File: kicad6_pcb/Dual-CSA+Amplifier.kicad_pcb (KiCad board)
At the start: 2 copper layers, 101 x 69.2 mm, 87 parts, among them J101 Direct2 In, J102 CSA2 In, J103 CSA1 In, J104 Direct1 In, J105 Bias In, J106 Direct in, J107 Direct in, J108 Output, J109 Output, J201 Barrel_Jack, J202 GND, J203 DC Power, J204 -8V, J205 +8V, J301 CA probe, J302 RV Prob, J401 CA probe, J402 RV Prob, U201 LM317L, U202 UA78M08, U203 UA79M08, U204 TLE2426xP, U301 CR110, U302 TL071, U401 CR110, U402 TL071

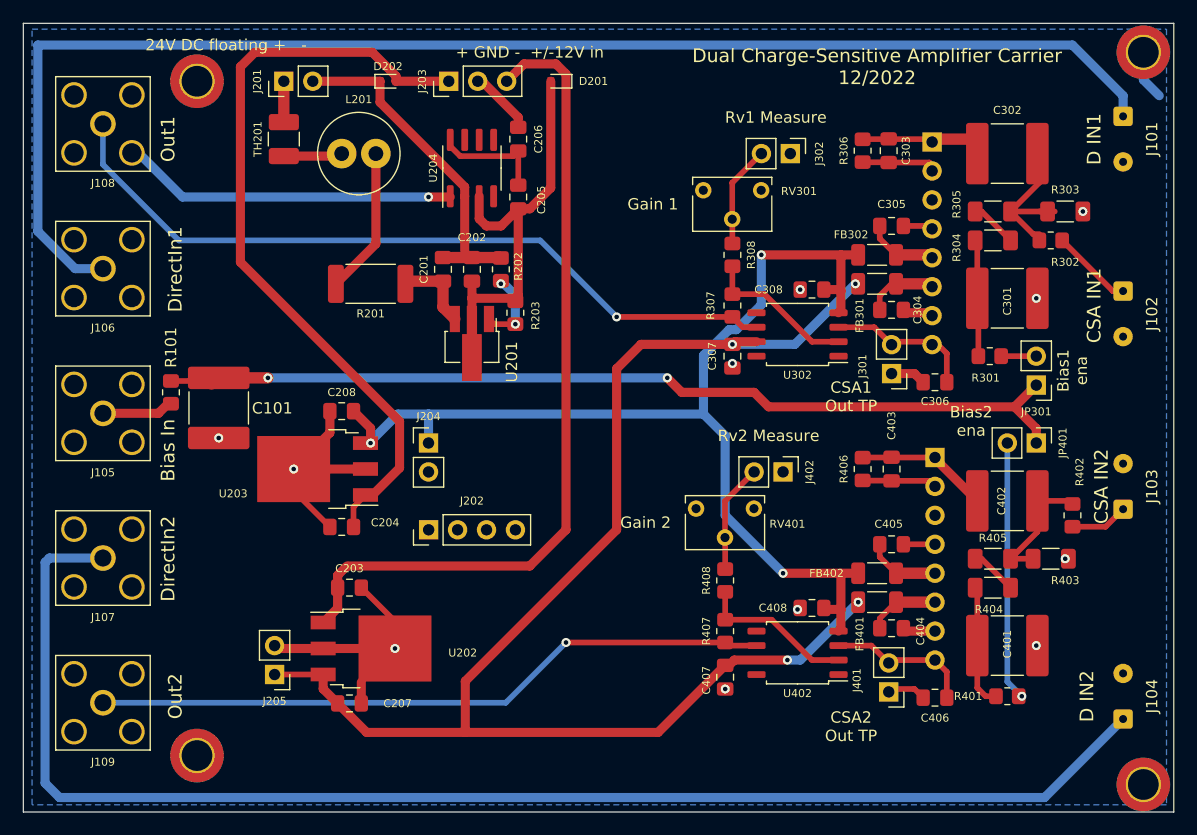
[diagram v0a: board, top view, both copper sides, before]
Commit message: CSA carrier v2. Multiple fixes and improvements.
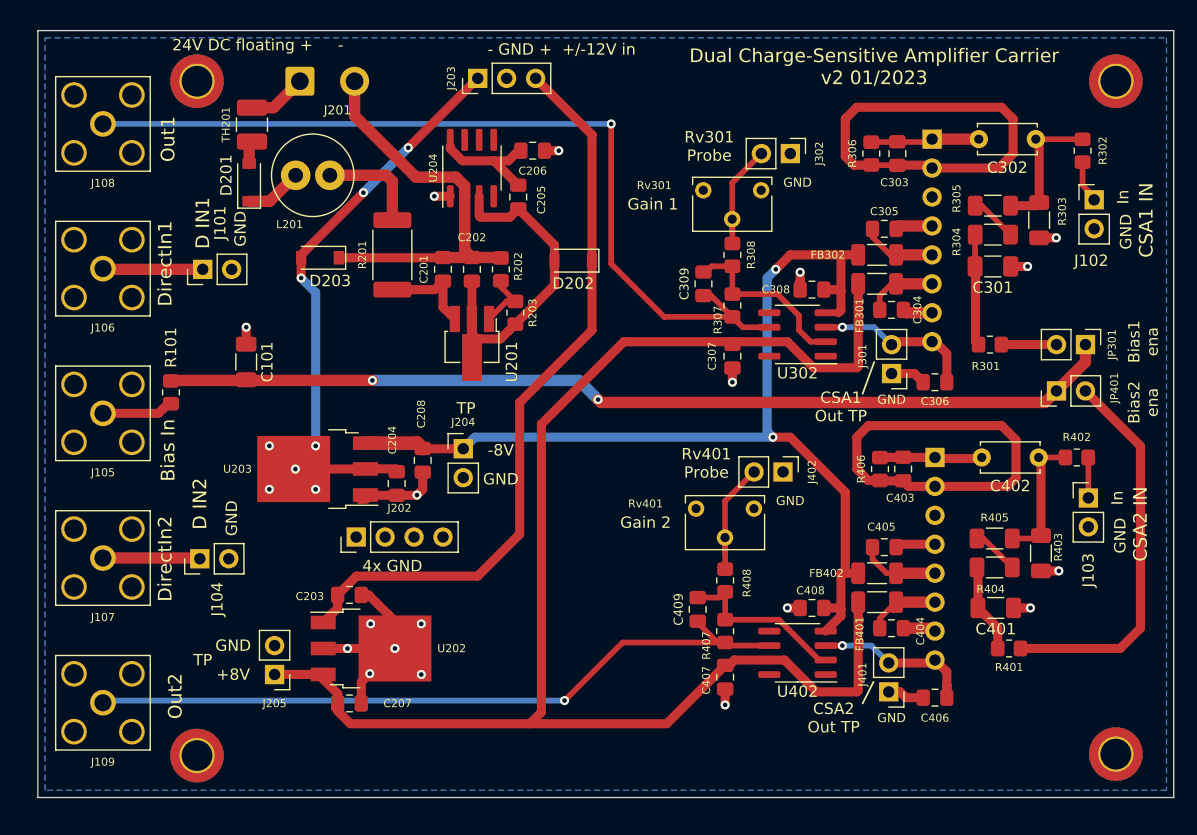
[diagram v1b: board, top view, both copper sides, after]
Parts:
- added C309: Open, Capacitor_SMD:C_0805_2012Metric_Pad1.18x1.45mm_HandSolder, F.Cu at (175.3, 114.3)
- added C409: Open, Capacitor_SMD:C_0805_2012Metric_Pad1.18x1.45mm_HandSolder, F.Cu at (174.8, 142.9)
- added D203: D, Diode_SMD:D_SOD-123, F.Cu at (141.6, 112.0)
- C101, C301, C401: footprint Capacitor_SMD:C_2220_5650Metric_Pad1.97x5.40mm_HandSolder -> Capacitor_SMD:C_1206_3216Metric_Pad1.33x1.80mm_HandSolder
- C302, C402: footprint Capacitor_SMD:C_2220_5650Metric_Pad1.97x5.40mm_HandSolder -> Capacitor_THT:C_Disc_D5.0mm_W2.5mm_P5.00mm
- D201, D202: value RB751V-40 -> D; footprint Diode_SMD:D_SOD-523 -> Diode_SMD:D_SOD-123
- J101, J102, J103, J104: footprint Connector_Wire:SolderWire-0.15sqmm_1x02_P4mm_D0.5mm_OD1.5mm -> Connector_PinHeader_2.54mm:PinHeader_1x02_P2.54mm_Vertical
- J201: footprint Connector_PinHeader_2.54mm:PinHeader_1x02_P2.54mm_Vertical -> Connector_Wire:SolderWire-0.75sqmm_1x02_P4.8mm_D1.25mm_OD2.3mm
- U302, U402: footprint Package_SO:SOIC-8_5.23x5.23mm_P1.27mm -> Package_SO:SOIC-8_3.9x4.9mm_P1.27mm
- moved J104 82.2 mm to (131.1, 138.4)
- moved J101 81.9 mm to (131.3, 113.0), turned to 90 degrees
- moved D201 28.6 mm to (135.4, 105.4), turned to 90 degrees
- moved D202 22.6 mm to (163.8, 112.3), turned to 180 degrees
- moved J102 8.40 mm to (209.6, 106.9), turned to 0 degrees
- moved R302 8.36 mm to (208.5, 102.6), turned to -90 degrees
- moved C208 8.32 mm to (150.6, 129.8), turned to -90 degrees
- moved J202 6.39 mm to (144.8, 136.5)
- moved C204 6.15 mm to (148.3, 131.8), turned to -90 degrees
- moved JP301 5.59 mm to (208.8, 119.6), turned to -90 degrees
- moved R402 5.09 mm to (208.0, 129.5), turned to 0 degrees
- moved JP401 4.90 mm to (206.2, 123.7), turned to 90 degrees
- moved C402 4.70 mm to (204.7, 129.5)
- moved C101 4.70 mm to (135.1, 121.2), turned to -90 degrees
- moved L201 4.47 mm to (139.5, 104.8)
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- renumbered RV301 to Rv301, RV401 to Rv401
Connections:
- D201 pad 1: Net-(C203-Pad1) -> Net-(D201-Pad1)
- D201 pad 2: Net-(C202-Pad1) -> Net-(D201-Pad2)
- D202 pad 1: Net-(C201-Pad2) -> Net-(C203-Pad1)
- D202 pad 2: Net-(C204-Pad1) -> Net-(C202-Pad1)
- L201 pad 1: Net-(L201-Pad1) -> Net-(D201-Pad1)
- TH201 pad 1: Net-(L201-Pad1) -> Net-(D201-Pad2)
- U203 pad 1: Net-(C204-Pad1) -> GND
- U203 pad 2: GND -> Net-(C204-Pad1)
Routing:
- net Net-(J104-Pad1): track 122.6 -> 8.31 mm
- net Net-(J101-Pad1): track 122.3 -> 8.69 mm
- net GND: track 106.1 -> 127.9 mm, vias 12 -> 18
- net Net-(JP401-Pad2): track 22.8 -> 34.1 mm, vias 1 -> 0
- net +8V: track 122.6 -> 132.9 mm, vias 4 -> 0
- net /CSA+Amp/Out: track 66.8 -> 76.4 mm
- net -8V: track 98.2 -> 90.1 mm, vias 3 -> 2
- net Net-(C202-Pad1): track 34.4 -> 27.2 mm
- net Net-(C204-Pad1): track 67.7 -> 75.0 mm, vias 0 -> 8
- net Net-(C201-Pad2): track 29.0 -> 35.7 mm
- net Net-(C203-Pad1): track 72.4 -> 65.8 mm
- net Net-(D201-Pad1): track 0.00 -> 5.03 mm
- net Net-(L201-Pad1): track 4.43 -> 0.00 mm
- net /CSA+Amp1/Out: track 59.0 -> 63.2 mm
- net Net-(L201-Pad2): track 12.9 -> 9.11 mm
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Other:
- board size 101 x 69.2 mm -> 99.7 x 67.3 mm
- board text added: "+8V"
- board text added: "- GND + +/-12V in"
- board text added: "-8V"
- board text added: "4x GND"
- board text added: "CSA1 IN"
- board text added: "CSA2 IN"
- board text added: "Dual Charge-Sensitive Amplifier Carrier v2 01/2023"
- board text added: "GND"
- board text added: "In"
- board text added: "Rv301 Probe"
- board text added: "Rv401 Probe"
- board text added: "TP"
- board text removed: "+ GND - +/-12V in"
- board text removed: "CSA IN1"
- board text removed: "CSA IN2"
- board text removed: "Dual Charge-Sensitive Amplifier Carrier 12/2022"
- board text removed: "Rv1 Measure"
- board text removed: "Rv2 Measure"
